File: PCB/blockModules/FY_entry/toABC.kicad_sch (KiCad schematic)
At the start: 3 parts, among them U1901 EL817S

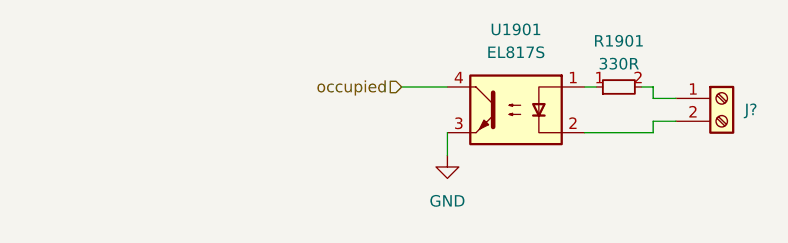
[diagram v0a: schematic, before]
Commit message: Added PDF files for all schematics
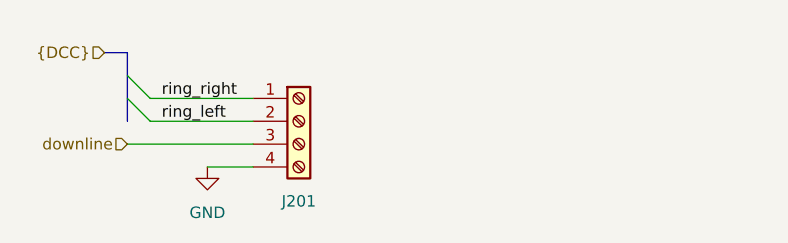
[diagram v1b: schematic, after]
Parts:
- removed J?: Screw_Terminal_01x02, Connector_Phoenix_MC:PhoenixContact_MC_1,5_2-G-3.5_1x02_P3.50mm_Horizontal, symbol Connector:Screw_Terminal_01x02
- removed R1901: 330R, custom_kicad_lib_sk:R_0603_smalltext, symbol resistors_0603:R_330R_0603
- removed U1901: EL817S, Package_DIP:SMDIP-4_W7.62mm, symbol custom_kicad_lib_sk:EL817S
- added J201: Screw_Terminal_01x04, Connector_Phoenix_MC:PhoenixContact_MC_1,5_4-G-3.5_1x04_P3.50mm_Horizontal, symbol Connector:Screw_Terminal_01x04
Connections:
- net GND: now also J201.4 (Pin_4)
- new net downline: J201.3 (Pin_3)
- new net ring_left: J201.2 (Pin_2)
- new net ring_right: J201.1 (Pin_1)
